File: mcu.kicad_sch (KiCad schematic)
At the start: 45 parts, among them IC5 3v3 LDO, J11 Conn_01x06_Female, U7 ESP32-C3, U8 SN74LV1T125DBVR, Y1 40 MHz

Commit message: Checkpoint before v120 changes
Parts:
- C16: value 1u -> C_1u_0603; Val (none) -> 1u
- C27, C29: value 16pF -> C_16p_0402; Val (none) -> 16p
- R136: value (none) -> R_0R_0402; footprint (none) -> Resistor_SMD:R_0402_1005Metric
- R64, R65: value R_2k2_0402 -> R_2k_0402; MPN CRCW040210K0FKEDHP -> (none); Manufacturer VISHAY -> (none); Val DNP -> 2k
- R75, R76, R77: value TBD -> R_2k_0402; Val TBD -> 2k
- R78, R82: value R_10K_0402 -> R_10k_0402; Val 10K -> 10k
- R79: value R_100K_0402 -> R_100k_0402; Val 100K -> 100k
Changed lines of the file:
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@@
       (effects (font (size 1.524 1.524)) (justify left))
     )
-    (property "Value" "TBD" (id 1) (at 124.46 124.46 0)
+    (property "Value" "R_2k_0402" (id 1) (at 124.46 124.46 0)
       (effects (font (size 1.524 1.524)) hide)
     )
@@
       (effects (font (size 1.27 1.27)) hide)
     )
-    (property "Val" "TBD" (id 6) (at 126.238 128.27 0)
+    (property "Val" "2k" (id 6) (at 126.238 128.27 0)
       (effects (font (size 1.27 1.27)) (justify left))
     )
@@
   )
   (symbol (lib_id "Device:C") (at 137.16 65.405 270) (unit 1)
-    (in_bom yes) (on_board yes) (fields_autoplaced)
-    (property "Reference" "C29" (id 0) (at 137.16 58.42 90))
-    (property "Value" "16pF" (id 1) (at 137.16 60.96 90))
+    (in_bom yes) (on_board yes)
+    (property "Reference" "C29" (id 0) (at 137.16 60.452 90))
+    (property "Value" "C_16p_0402" (id 1) (at 137.16 60.96 90)
+      (effects (font (size 1.27 1.27)) hide)
+    )
     (property "Footprint" "Capacitor_SMD:C_0402_1005Metric" (id 2) (at 133.35 66.3702 0)
       (effects (font (size 1.27 1.27)) hide)
@@
       (effects (font (size 1.27 1.27)) hide)
     )
+    (property "Val" "16p" (id 4) (at 137.16 61.976 90))
     (pin "1")
     (pin "2")
@@
   )
   (symbol (lib_id "Device:C") (at 137.16 55.245 270) (unit 1)
-    (in_bom yes) (on_board yes) (fields_autoplaced)
-    (property "Reference" "C27" (id 0) (at 137.16 48.26 90))
-    (property "Value" "16pF" (id 1) (at 137.16 50.8 90))
+    (in_bom yes) (on_board yes)
+    (property "Reference" "C27" (id 0) (at 137.16 49.911 90))
+    (property "Value" "C_16p_0402" (id 1) (at 137.16 50.8 90)
+      (effects (font (size 1.27 1.27)) hide)
+    )
     (property "Footprint" "Capacitor_SMD:C_0402_1005Metric" (id 2) (at 133.35 56.2102 0)
       (effects (font (size 1.27 1.27)) hide)
@@
       (effects (font (size 1.27 1.27)) hide)
     )
+    (property "Val" "16p" (id 4) (at 137.16 51.689 90))
     (pin "1")
     (pin "2")
@@
       (effects (font (size 1.524 1.524)) (justify left))
     )
-    (property "Value" "R_10K_0402" (id 1) (at 252.73 87.63 0)
+    (property "Value" "R_10k_0402" (id 1) (at 252.73 87.63 0)
       (effects (font (size 1.524 1.524)) hide)
     )
@@
       (effects (font (size 1.27 1.27)) hide)
     )
-    (property "Val" "10K" (id 6) (at 254.508 91.44 0)
+    (property "Val" "10k" (id 6) (at 254.508 91.44 0)
       (effects (font (size 1.27 1.27)) (justify left))
     )
@@
       (effects (font (size 1.524 1.524)) (justify left))
     )
-    (property "Value" "R_100K_0402" (id 1) (at 252.73 92.71 0)
+    (property "Value" "R_100k_0402" (id 1) (at 252.73 92.71 0)
       (effects (font (size 1.524 1.524)) hide)
     )
@@
       (effects (font (size 1.27 1.27)) hide)
     )
-    (property "Val" "100K" (id 6) (at 255.27 96.52 0)
+    (property "Val" "100k" (id 6) (at 255.27 96.52 0)
       (effects (font (size 1.27 1.27)) (justify left))
     )
@@
       (effects (font (size 1.524 1.524)) (justify left))
     )
-    (property "Value" "TBD" (id 1) (at 124.46 127 0)
+    (property "Value" "R_2k_0402" (id 1) (at 124.46 127 0)
       (effects (font (size 1.524 1.524)) hide)
     )
@@
       (effects (font (size 1.27 1.27)) hide)
     )
-    (property "Val" "TBD" (id 6) (at 126.238 130.81 0)
+    (property "Val" "2k" (id 6) (at 126.238 130.81 0)
       (effects (font (size 1.27 1.27)) (justify left))
     )
@@
       (effects (font (size 1.524 1.524)) (justify left))
     )
-    (property "Value" "R_10K_0402" (id 1) (at 267.97 113.03 0)
+    (property "Value" "R_10k_0402" (id 1) (at 267.97 113.03 0)
       (effects (font (size 1.524 1.524)) hide)
     )
@@
       (effects (font (size 1.27 1.27)) hide)
     )
-    (property "Val" "10K" (id 6) (at 269.748 116.84 0)
+    (property "Val" "10k" (id 6) (at 269.748 116.84 0)
       (effects (font (size 1.27 1.27)) (justify left))
     )
@@
     (in_bom yes) (on_board yes)
     (property "Reference" "C16" (id 0) (at 277.495 88.646 0))
-    (property "Value" "1u" (id 1) (at 278.638 91.186 0))
+    (property "Value" "C_1u_0603" (id 1) (at 278.638 91.186 0)
+      (effects (font (size 1.27 1.27)) hide)
+    )
     (property "Footprint" "Capacitor_SMD:C_0603_1608Metric" (id 2) (at 275.7932 94.996 0)
       (effects (font (size 1.27 1.27)) hide)
@@
       (effects (font (size 1.27 1.27)) hide)
     )
+    (property "Val" "1u" (id 4) (at 278.511 91.186 0))
     (pin "1")
     (pin "2")
@@
       (effects (font (size 1.524 1.524)) (justify left))
     )
-    (property "Value" "" (id 1) (at 262.001 68.834 0)
-      (effects (font (size 1.524 1.524)) hide)
-    )
-    (property "Footprint" "" (id 2) (at 256.921 77.724 0)
+    (property "Value" "R_0R_0402" (id 1) (at 262.001 68.834 0)
+      (effects (font (size 1.524 1.524)) hide)
+    )
+    (property "Footprint" "Resistor_SMD:R_0402_1005Metric" (id 2) (at 256.921 77.724 0)
       (effects (font (size 1.524 1.524)) (justify left) hide)
     )
@@
       (effects (font (size 1.524 1.524)) (justify left))
     )
-    (property "Value" "TBD" (id 1) (at 124.46 129.54 0)
+    (property "Value" "R_2k_0402" (id 1) (at 124.46 129.54 0)
       (effects (font (size 1.524 1.524)) hide)
     )
@@
       (effects (font (size 1.27 1.27)) hide)
     )
-    (property "Val" "TBD" (id 6) (at 126.238 133.35 0)
+    (property "Val" "2k" (id 6) (at 126.238 133.35 0)
       (effects (font (size 1.27 1.27)) (justify left))
     )
@@
       (effects (font (size 1.524 1.524)) (justify left))
     )
-    (property "Value" "R_2k2_0402" (id 1) (at 161.925 69.85 0)
+    (property "Value" "R_2k_0402" (id 1) (at 161.925 69.85 0)
       (effects (font (size 1.524 1.524)) hide)
     )
@@
       (effects (font (size 1.27 1.27)) hide)
     )
-    (property "Manufacturer" "VISHAY" (id 4) (at 156.845 83.82 0)
-      (effects (font (size 1.524 1.524)) (justify left) hide)
-    )
-    (property "MPN" "CRCW040210K0FKEDHP" (id 5) (at 156.845 81.28 0)
-      (effects (font (size 1.524 1.524)) (justify left) hide)
-    )
-    (property "Val" "DNP" (id 6) (at 163.703 73.66 0)
+    (property "Val" "2k" (id 6) (at 163.703 73.66 0)
       (effects (font (size 1.27 1.27)) (justify left))
     )
@@
       (effects (font (size 1.524 1.524)) (justify left))
     )
-    (property "Value" "R_2k2_0402" (id 1) (at 161.925 67.31 0)
+    (property "Value" "R_2k_0402" (id 1) (at 161.925 67.31 0)
       (effects (font (size 1.524 1.524)) hide)
     )
@@
       (effects (font (size 1.27 1.27)) hide)
     )
-    (property "Manufacturer" "VISHAY" (id 4) (at 156.845 81.28 0)
-      (effects (font (size 1.524 1.524)) (justify left) hide)
-    )
-    (property "MPN" "CRCW040210K0FKEDHP" (id 5) (at 156.845 78.74 0)
-      (effects (font (size 1.524 1.524)) (justify left) hide)
-    )
-    (property "Val" "DNP" (id 6) (at 163.703 71.12 0)
-      (effects (font (size 1.27 1.27)) (justify left))
-    )
+    (property "Val" "2k" (id 6) (at 163.703 71.12 0)
+      (effects (font (size 1.27 1.27)) (justify left))
+    )

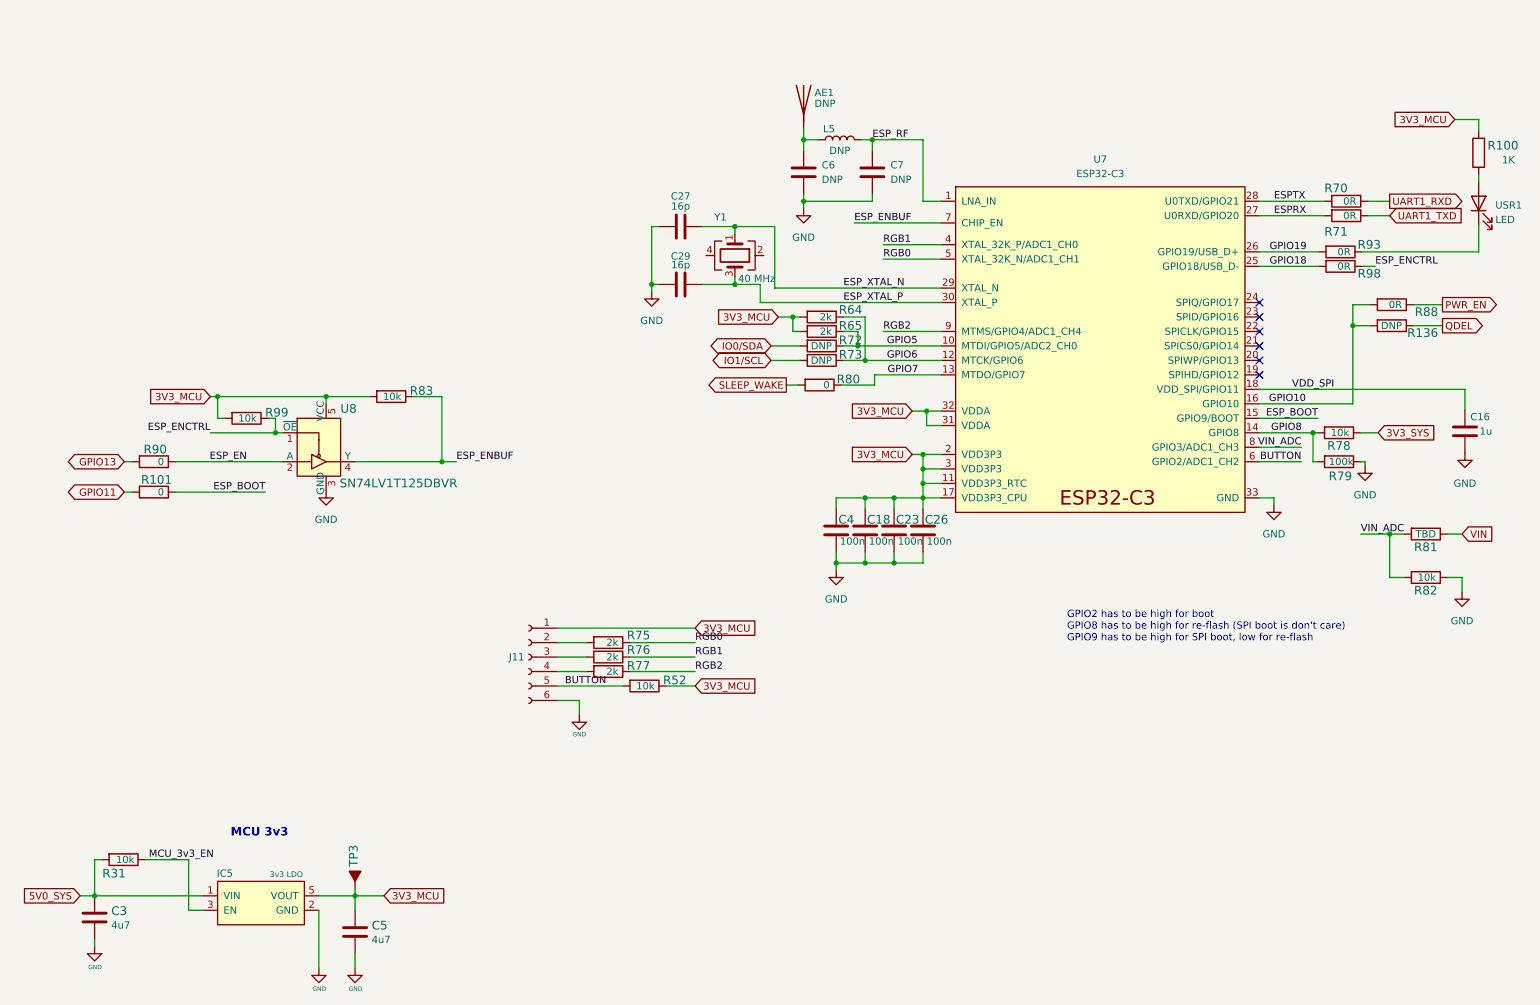
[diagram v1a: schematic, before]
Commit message: Fix #11 and move NAND gate to 3v3
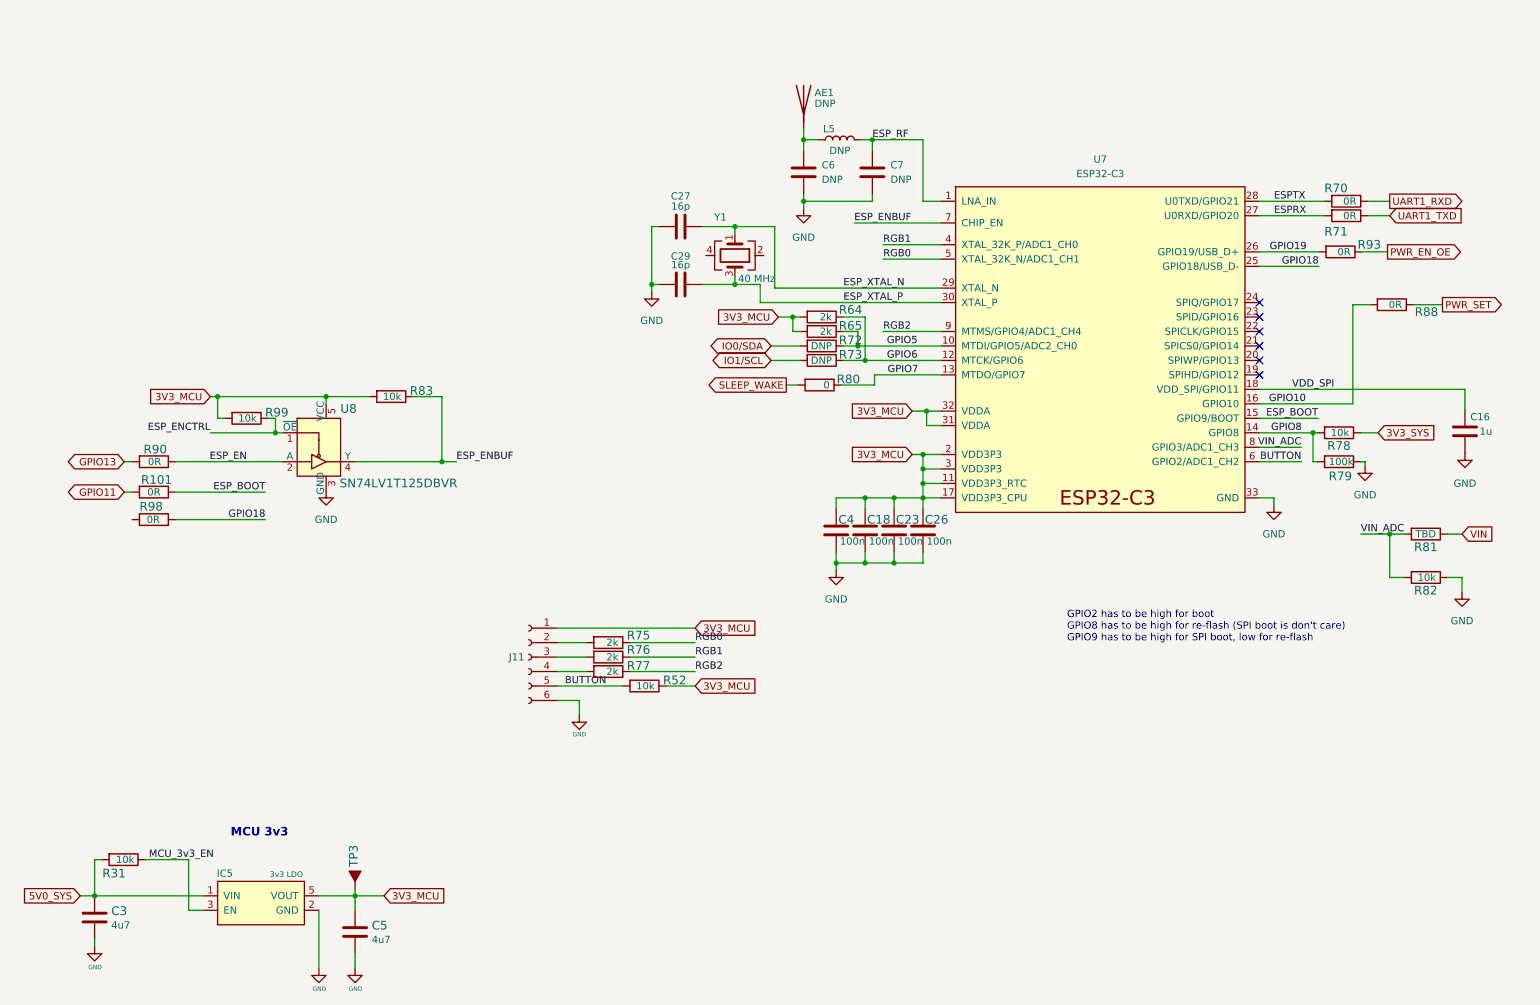
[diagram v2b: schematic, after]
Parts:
- removed R100: R_1K_0402, Resistor_SMD:R_0402_1005Metric, symbol jetson-nano-baseboard:R_220R_0402
- removed R136: R_0R_0402, Resistor_SMD:R_0402_1005Metric, symbol jetson-nano-baseboard:R_10k_0402
- removed USR1: LED, LED_SMD:LED_0603_1608Metric, symbol Device:LED
- R101, R90: Val 0 -> 0R
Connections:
- net ESP_ENCTRL: no longer R98.1
- net PWR_EN_OE: now reaches R93.1
- net PWR_EN renamed PWR_SET
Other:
- moved on the sheet: R98

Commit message: Resolve #4 - level shifter now on UART, also used to isolate MCU BOOT and EN
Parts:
- removed R101, R98: R_0R_0402, Resistor_SMD:R_0402_1005Metric, symbol jetson-nano-baseboard:R_10k_0402
- removed R99: R_10k_0402, Resistor_SMD:R_0402_1005Metric, symbol jetson-nano-baseboard:R_10k_0402
- removed U8: SN74LV1T125DBVR, jetson-nano-baseboard-footprints:SOT-23-5, symbol jetson-nano-baseboard:SN74LV1T125DBVR
- added C50, C53: C_100n_0402, Capacitor_SMD:C_0402_1005Metric, symbol jetson-nano-baseboard:C_100n_0402
- added C54: C_10u_0603, jetson-nano-baseboard-footprints:0603-cap, symbol jetson-nano-baseboard:C_10u_0603
- added U8: TXU0304BQA, capablerobot-footprints:TXU0304BQAR, symbol capablerobot-io:TXU0304BQA
- C18, C23, C26: footprint jetson-nano-baseboard-footprints:0402-cap -> Capacitor_SMD:C_0402_1005Metric
- C4: footprint jetson-nano-baseboard-footprints:0402-cap -> Capacitor_SMD:C_0402_1005Metric; MPN 0402X104K6R3CT -> (none); Manufacturer Walsin -> (none)
- R70, R71: value R_0R_0402 -> R_10k_0402; Val 0R -> 10k
- R90: value R_0R_0402 -> R_100k_0402; Val 0R -> 100k
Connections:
- net ESP_ENBUF is gone; now on net ESP_EN: R83.1, U7.7 (CHIP_EN)
- net 3V3_MCU: now also R71.2, C53.2, U8.14 (VCCB)
- net ESP_BOOT: now also R71.1, U8.12 (B2Y)
- net ESP_EN: now also U8.13 (B1Y); no longer R90.1
- net GND: now also R70.2, C50.1, C53.1, C54.1, U8.15 (PAD), U8.7 (GND)
- net GPIO11: now also U8.3 (A2)
- net GPIO13: now also U8.2 (A1); no longer R90.2
- net IO0/SDA: now also R73.2; no longer R72.2
- net IO1/SCL: now also R72.2; no longer R73.2
- net UART1_RXD: now also U8.5 (A4Y); no longer R70.1
- net UART1_TXD: now also U8.4 (A3); no longer R71.1
- net ESPRX renamed ESP_RX
- net ESP_RX: now also U8.11 (B3Y); no longer R71.2
- net ESPTX renamed ESP_TX
- net ESP_TX: now also U8.10 (B4); no longer R70.2
- net GPIO18: no longer names the net of U7.25 (GPIO18/USB_D-)
- new net 1V8_SYS: C50.2, U8.1 (VCCA)
- new net BUF_EN: C54.2, R70.1, R90.2, U8.8 (OE)
- new net GPIO04: R90.1
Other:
- moved on the sheet: R83, R88

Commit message: Resolve #14 by adding edge debug interface to MCU.  Change test pads and ESD parts.
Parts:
- removed R79: R_100k_0402, Resistor_SMD:R_0402_1005Metric, symbol jetson-nano-baseboard:R_10k_0402
- added J18: DebugEdge_02x03, capablerobot-footprints:DebugEdge_2x03_Target, symbol Connector_DebugEdge:DebugEdge_02x03
- added Q5: BSS138APW, jetson-nano-baseboard-footprints:SC70-3, symbol jetson-nano-baseboard:BSS138APW
- added R137: R_10k_0402, Resistor_SMD:R_0402_1005Metric, symbol jetson-nano-baseboard:R_10k_0402
- added R141: R_0R_0402, Resistor_SMD:R_0402_1005Metric, symbol jetson-nano-baseboard:R_10k_0402
- added U9: TPD4E05U06DQAR, Package_SON:USON-10_2.5x1.0mm_P0.5mm, symbol Power_Protection:TPD4E02B04DQA
- R78: value R_10k_0402 -> R_100k_0402; Val 10k -> 100k
- TP3: footprint jetson-nano-baseboard-footprints:TP-R-1.5 -> TestPoint:TestPoint_Pad_D1.0mm
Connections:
- net 3V3_MCU: now also R78.1, R141.2
- net 3V3_SYS: now also R137.1; no longer R78.1
- net ESP_BOOT: now also J18.2 (SWDIO/TMS), U9.2 (IO2)
- net ESP_EN: now also J18.4 (~{RESET}), U9.4 (IO3)
- net ESP_RX: now also J18.3 (SWDCLK/TCLK), U9.5 (IO4)
- net ESP_TX: now also J18.6 (SWO/TDO), U9.1 (IO1)
- net GND: now also J18.1 (GND), Q5.2 (S), U9.3 (G), U9.8 (G)
- net GPIO8: now also Q5.3 (D)
- net RGB0: now also U7.4 (XTAL_32K_P/ADC1_CH0); no longer U7.5 (XTAL_32K_N/ADC1_CH1)
- net RGB1: now also U7.5 (XTAL_32K_N/ADC1_CH1); no longer U7.4 (XTAL_32K_P/ADC1_CH0)
- new net: Q5.1 (G), R137.2
- new net: J18.5 (Vref), R141.1
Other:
- moved on the sheet: J11, R52, R75, R76, R77

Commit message: Change FPGA to ICE40UP5K
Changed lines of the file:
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@@
-    )
-  )
-  (global_label "3V3_SYS" (shape input) (at 264.795 69.596 0) (fields_autoplaced)
-    (effects (font (size 1.27 1.27)) (justify left))
-    (property "Intersheet References" "${INTERSHEET_REFS}" (id 0) (at 275.1021 69.5166 0)
-      (effects (font (size 1.27 1.27)) (justify left) hide)
     )
   )
